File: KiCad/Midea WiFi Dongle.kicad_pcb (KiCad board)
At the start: 4 copper layers, 20 x 48.5 mm, 21 parts, among them J1 USB_A, Q1 BSS138, Q2 BSS138, SW1 PRG, SW2 RST, U1 LM1117-3.3, U2 ESP-12F

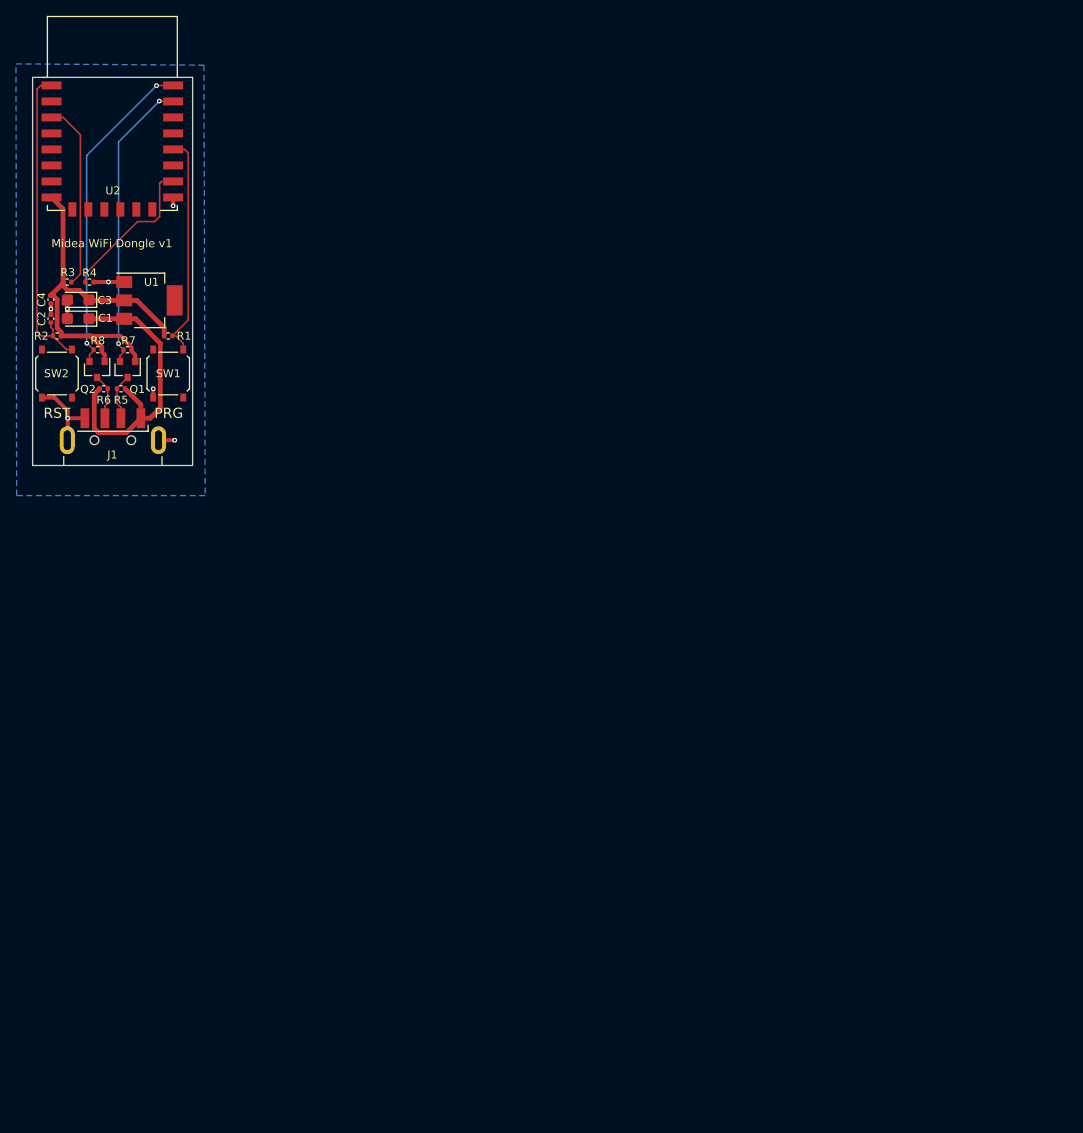
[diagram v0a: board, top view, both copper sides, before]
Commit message: Added v2 adjusted to EU-SK105
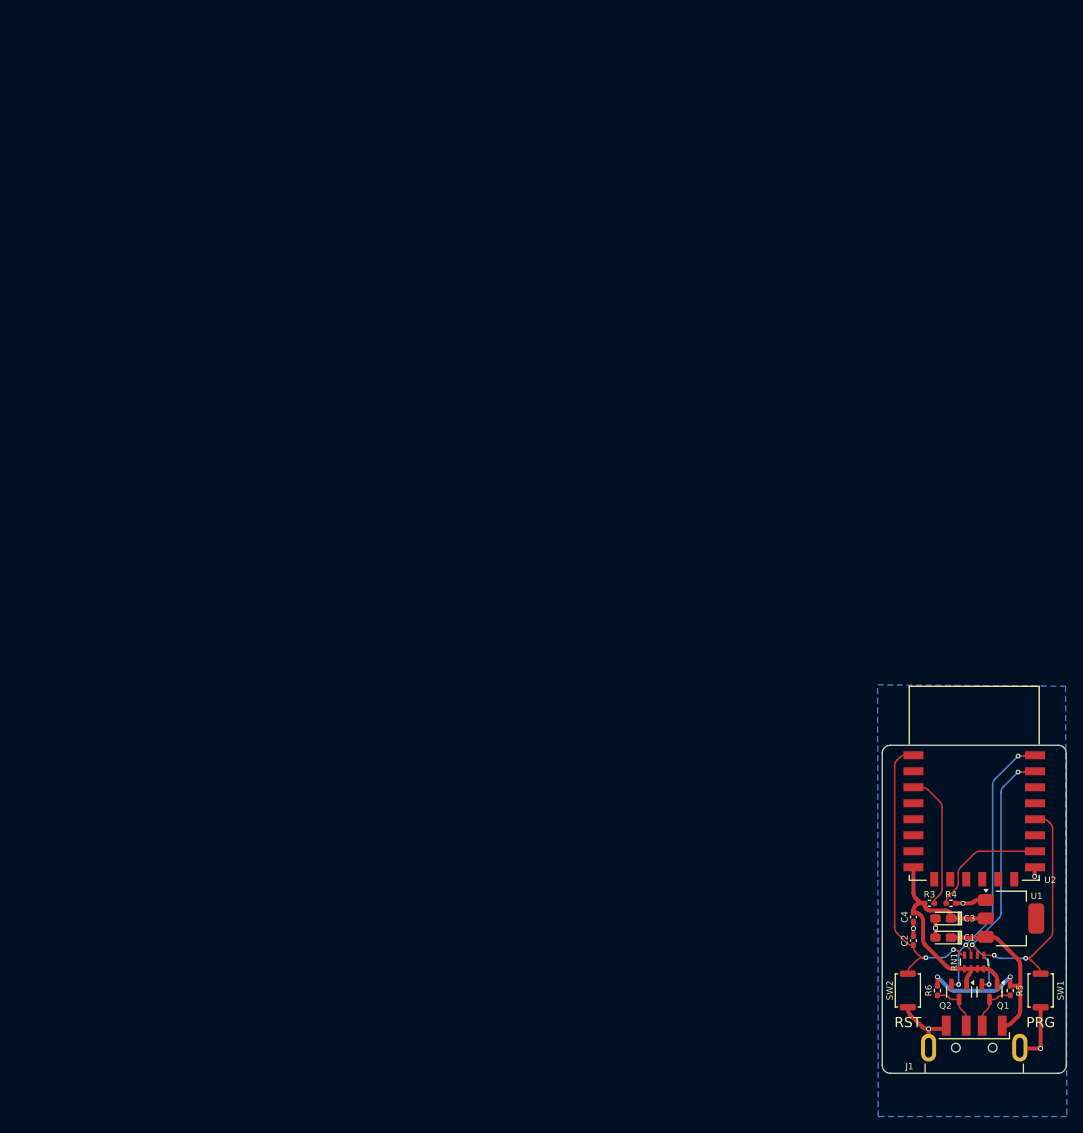
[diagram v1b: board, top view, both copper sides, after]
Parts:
- removed R1, R2, R7, R8: 10k, Resistor_SMD:R_0402_1005Metric
- added G1: LOGO, Andys-Footprints:Yoshi-Egg-Small, B.Cu at (153.9, 104.9)
- added RN1: R_Pack04, Resistor_SMD:R_Array_Concave_4x0603, F.Cu at (153.9, 110.7)
- C1, C3: value 47uF -> 10uF; footprint Capacitor_Tantalum_SMD:CP_EIA-3216-10_Kemet-I -> Andys-Footprints:CP_EIA-2012-12_Kemet-R_Pad1.30x1.05mm_HandSolder
- C2: value 470uF -> 470pF; footprint Capacitor_SMD:C_0402_1005Metric -> Capacitor_SMD:C_0402_1005Metric_Pad0.74x0.62mm_HandSolder
- C4: footprint Capacitor_SMD:C_0402_1005Metric -> Capacitor_SMD:C_0402_1005Metric_Pad0.74x0.62mm_HandSolder
- R3, R4, R5, R6: footprint Resistor_SMD:R_0402_1005Metric -> Resistor_SMD:R_0402_1005Metric_Pad0.72x0.64mm_HandSolder
- SW1: value PRG -> SW_Push; footprint mine:TS1187AXXX -> Button_Switch_SMD:SW_Push_SPST_NO_Alps_SKRK
- SW2: value RST -> SW_Push; footprint mine:TS1187AXXX -> Button_Switch_SMD:SW_Push_SPST_NO_Alps_SKRK
- U1: value LM1117-3.3 -> AMS1117-3.3
- moved U2 136.4 mm to (153.9, 88.3)
- moved REF** 134.7 mm to (153.9, 88.3)
- moved R5 134.2 mm to (158.4, 114.2), turned to -90 degrees
- moved SW1 133.6 mm to (162.2, 114.2)
- moved C1 133.0 mm to (150.0, 107.6)
- moved C3 132.9 mm to (150.0, 105.2)
- moved C2 132.9 mm to (146.3, 108.0)
- moved Q1 132.9 mm to (155.8, 114.4)
- moved Q2 132.9 mm to (152.0, 114.4)
- moved R3 132.8 mm to (148.3, 103.3)
- moved R4 132.8 mm to (151.0, 103.3)
- moved C4 132.6 mm to (146.3, 105.0)
- moved REF** 132.6 mm to (153.9, 113.4)
- moved U1 132.5 mm to (158.5, 105.2)
- moved J1 131.8 mm to (153.9, 128.2)
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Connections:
- net /RX renamed /RN1-6
- net /RX_APPLIANCE renamed /TX_USB
- net /TX renamed /RN1-5
- net /TX_APPLIANCE renamed /RX_USB
- U2 pad 10: Net-(U2-Pad10) -> unconnected-(U2-MISO-Pad10)
- U2 pad 11: Net-(U2-Pad11) -> unconnected-(U2-GPIO9-Pad11)
- U2 pad 12: Net-(U2-Pad12) -> unconnected-(U2-GPIO10-Pad12)
- U2 pad 13: Net-(U2-Pad13) -> unconnected-(U2-MOSI-Pad13)
- U2 pad 14: Net-(U2-Pad14) -> unconnected-(U2-SCLK-Pad14)
- U2 pad 17: Net-(U2-Pad17) -> unconnected-(U2-GPIO2-Pad17)
- U2 pad 19: Net-(U2-Pad19) -> unconnected-(U2-GPIO4-Pad19)
- U2 pad 2: Net-(U2-Pad2) -> unconnected-(U2-ADC-Pad2)
- U2 pad 20: Net-(U2-Pad20) -> unconnected-(U2-GPIO5-Pad20)
- U2 pad 4: Net-(U2-Pad4) -> unconnected-(U2-GPIO16-Pad4)
- U2 pad 5: Net-(U2-Pad5) -> unconnected-(U2-GPIO14-Pad5)
- U2 pad 6: Net-(U2-Pad6) -> unconnected-(U2-GPIO12-Pad6)
- U2 pad 7: Net-(U2-Pad7) -> unconnected-(U2-GPIO13-Pad7)
- U2 pad 9: Net-(U2-Pad9) -> unconnected-(U2-CS0-Pad9)
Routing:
- net +3V3: track 51.7 -> 34.6 mm
- net /EN: track 23.5 -> 16.9 mm
- net /RN1-5: track 40.8 -> 36.0 mm, vias 2 -> 3
- net +5V: track 37.9 -> 33.2 mm, vias 0 -> 2
- net /GPIO15: track 19.4 -> 15.2 mm
- net GND: track 22.3 -> 25.5 mm, vias 7 -> 6
- net /RN1-6: track 36.8 -> 34.2 mm, vias 2 -> 3
- net /RESET: track 39.5 -> 37.9 mm, vias 0 -> 2
- net /GPIO0: track 29.5 -> 28.8 mm, vias 0 -> 2
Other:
- board size 20 x 48.5 mm -> 23 x 41 mm
- copper layers 4 -> 2
- net class Default removed
- net class VCC removed
- board text added: "Midea WiFi Dongle v2"
- board text added: "Original Design by René Klootwijk (2020)"
- board text added: "v2 Changes by Andy (2025)"
- board text removed: "Copyright (C) 2020 René Klootwijk"
- board text removed: "Midea WiFi Dongle v1"
- board text removed: "PRG"
- board text removed: "RST"

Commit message: Added files for v2r1; updated ReadMe
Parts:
- removed C4: 100nF, Capacitor_SMD:C_0402_1005Metric_Pad0.74x0.62mm_HandSolder
- C1: value 10uF -> 22uF
- C2: value 470pF -> 22uF; footprint Capacitor_SMD:C_0402_1005Metric_Pad0.74x0.62mm_HandSolder -> Andys-Footprints:CP_EIA-2012-12_Kemet-R_Pad1.30x1.05mm_HandSolder
- C3: value 10uF -> 100nF; footprint Andys-Footprints:CP_EIA-2012-12_Kemet-R_Pad1.30x1.05mm_HandSolder -> Capacitor_SMD:C_0402_1005Metric_Pad0.74x0.62mm_HandSolder
- moved C2 4.64 mm to (150.0, 105.2), turned to 180 degrees
- moved C3 3.73 mm to (146.3, 105.0), turned to 90 degrees
- moved J1 0.45 mm to (153.9, 128.7)
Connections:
- C2 pad 1: /RESET -> +3V3
- C3 pad 1: +3V3 -> GND
- C3 pad 2: GND -> +3V3
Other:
- board text added: "Midea WiFi Dongle v2r1"
- board text removed: "Midea WiFi Dongle v2"

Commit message: Updated iBOM
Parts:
- RN1: value R_Pack04 -> 10k
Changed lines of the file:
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@@
 			)
 		)
-		(property "Description" "ESP-07 & ESP-08 can also be used"
+		(property "Description" ""
 			(at 0 0 0)
 			(unlocked yes)
@@
 			)
 		)
-		(property "Datasheet" ""
+		(property "Datasheet" "~"
 			(at 0 0 180)
 			(unlocked yes)
@@
 			)
 		)
-		(property "Description" "Can be ceramic or tantalum"
+		(property "Description" "Can be ceramic or tantalum, 2012 metric equals 0805 imperial"
 			(at 0 0 180)
 			(unlocked yes)
@@
 			)
 		)
-		(property "Datasheet" ""
+		(property "Datasheet" "~"
 			(at 0 0 180)
 			(layer "F.Fab")
@@
 			)
 		)
-		(property "Datasheet" ""
+		(property "Datasheet" "~"
 			(at 0 0 0)
 			(layer "F.Fab")
@@
 			)
 		)
-		(property "Datasheet" ""
+		(property "Datasheet" "~"
 			(at 0 0 270)
 			(layer "F.Fab")
@@
 			)
 		)
-		(property "Datasheet" ""
+		(property "Datasheet" "~"
 			(at 0 0 270)
 			(layer "F.Fab")
@@
 			)
 		)
-		(property "Datasheet" ""
+		(property "Datasheet" "~"
 			(at 0 0 270)
 			(unlocked yes)
@@
 			)
 		)
-		(property "Datasheet" ""
+		(property "Datasheet" "~"
 			(at 0 0 0)
 			(layer "F.Fab")
@@
 			)
 		)
-		(property "Description" "Can be ceramic or tantalum"
+		(property "Description" "Can be ceramic or tantalum, 2012 metric equals 0805 imperial"
 			(at 0 0 0)
 			(layer "F.Fab")
@@
 			)
 		)
-		(property "Datasheet" ""
+		(property "Datasheet" "~"
 			(at 0 0 90)
 			(unlocked yes)
@@
 			)
 		)
-		(property "Datasheet" ""
+		(property "Datasheet" "~"
 			(at 0 0 90)
 			(layer "F.Fab")
@@
 			)
 		)
-		(property "Value" "R_Pack04"
+		(property "Value" "10k"
 			(at 0 2.6 90)
 			(layer "F.Fab")
@@
 			)
 		)
-		(property "Datasheet" ""
+		(property "Datasheet" "~"
 			(at 0 0 90)
 			(unlocked yes)
@@
 			)
 		)
-		(property "Datasheet" ""
+		(property "Datasheet" "~"
 			(at 0 0 90)
 			(unlocked yes)
